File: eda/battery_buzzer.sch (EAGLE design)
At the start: 28 parts, among them Q2 IRFML8244, U1 ISL83491SOIC, U2 ATTINY1634

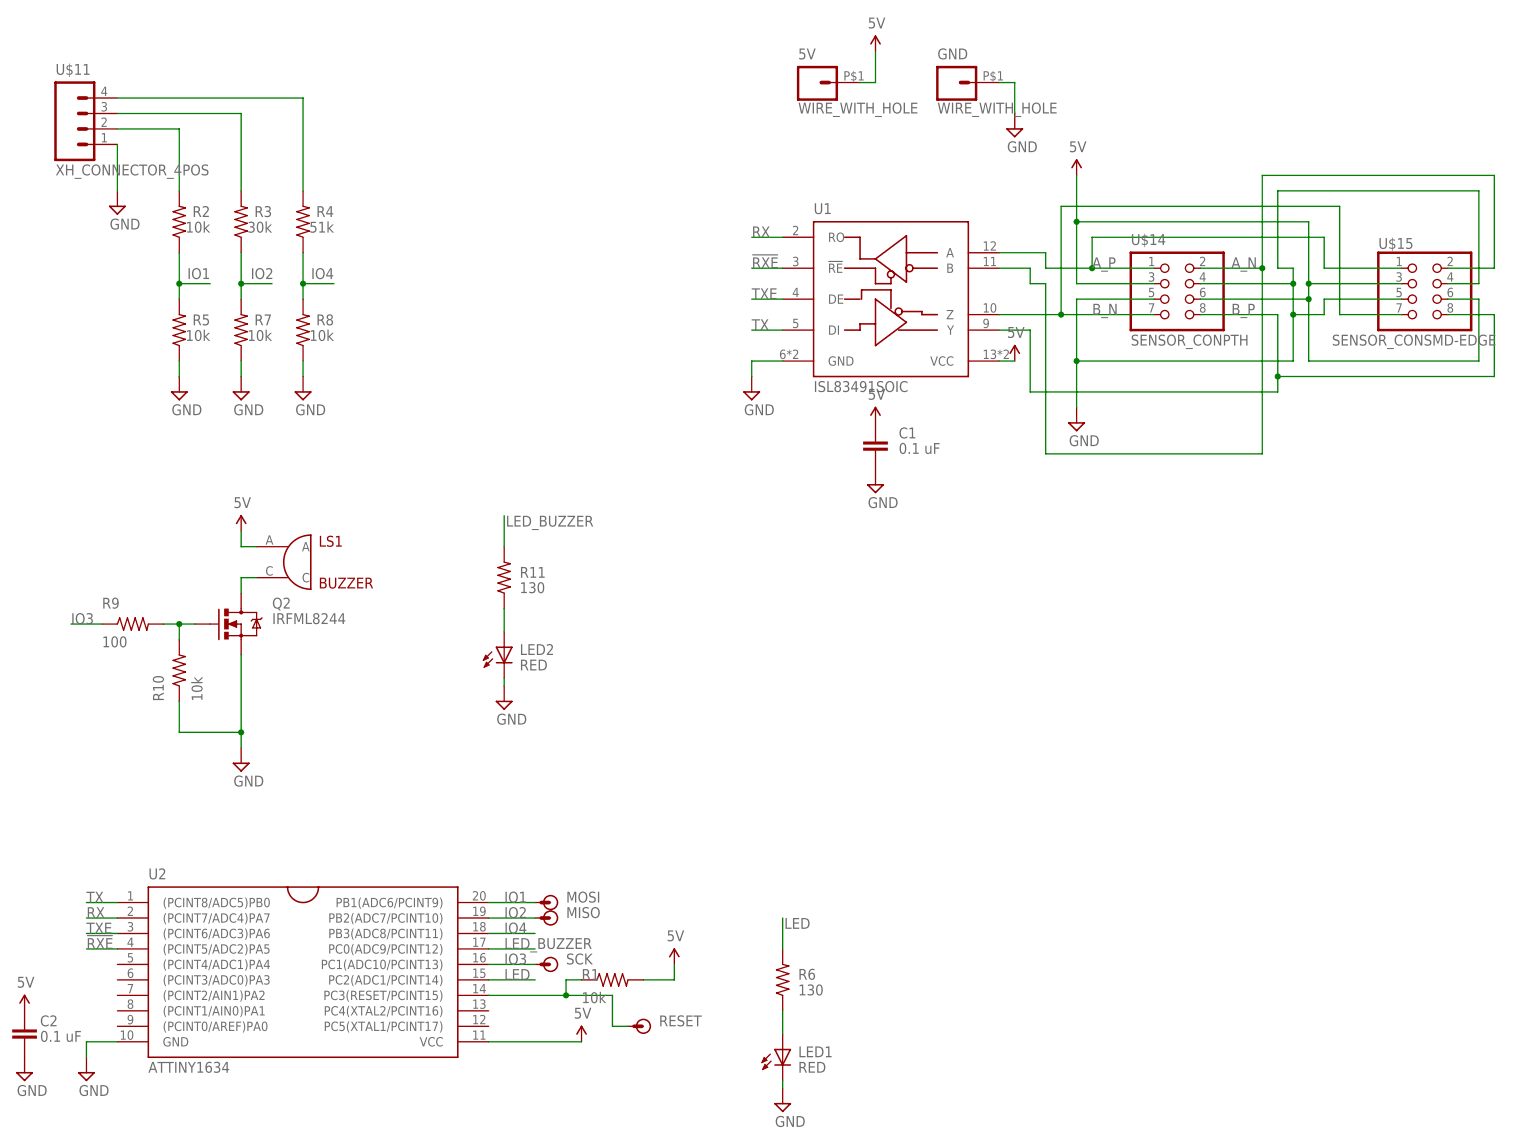
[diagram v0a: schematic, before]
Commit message: Change smartsensor connectors to 2x5
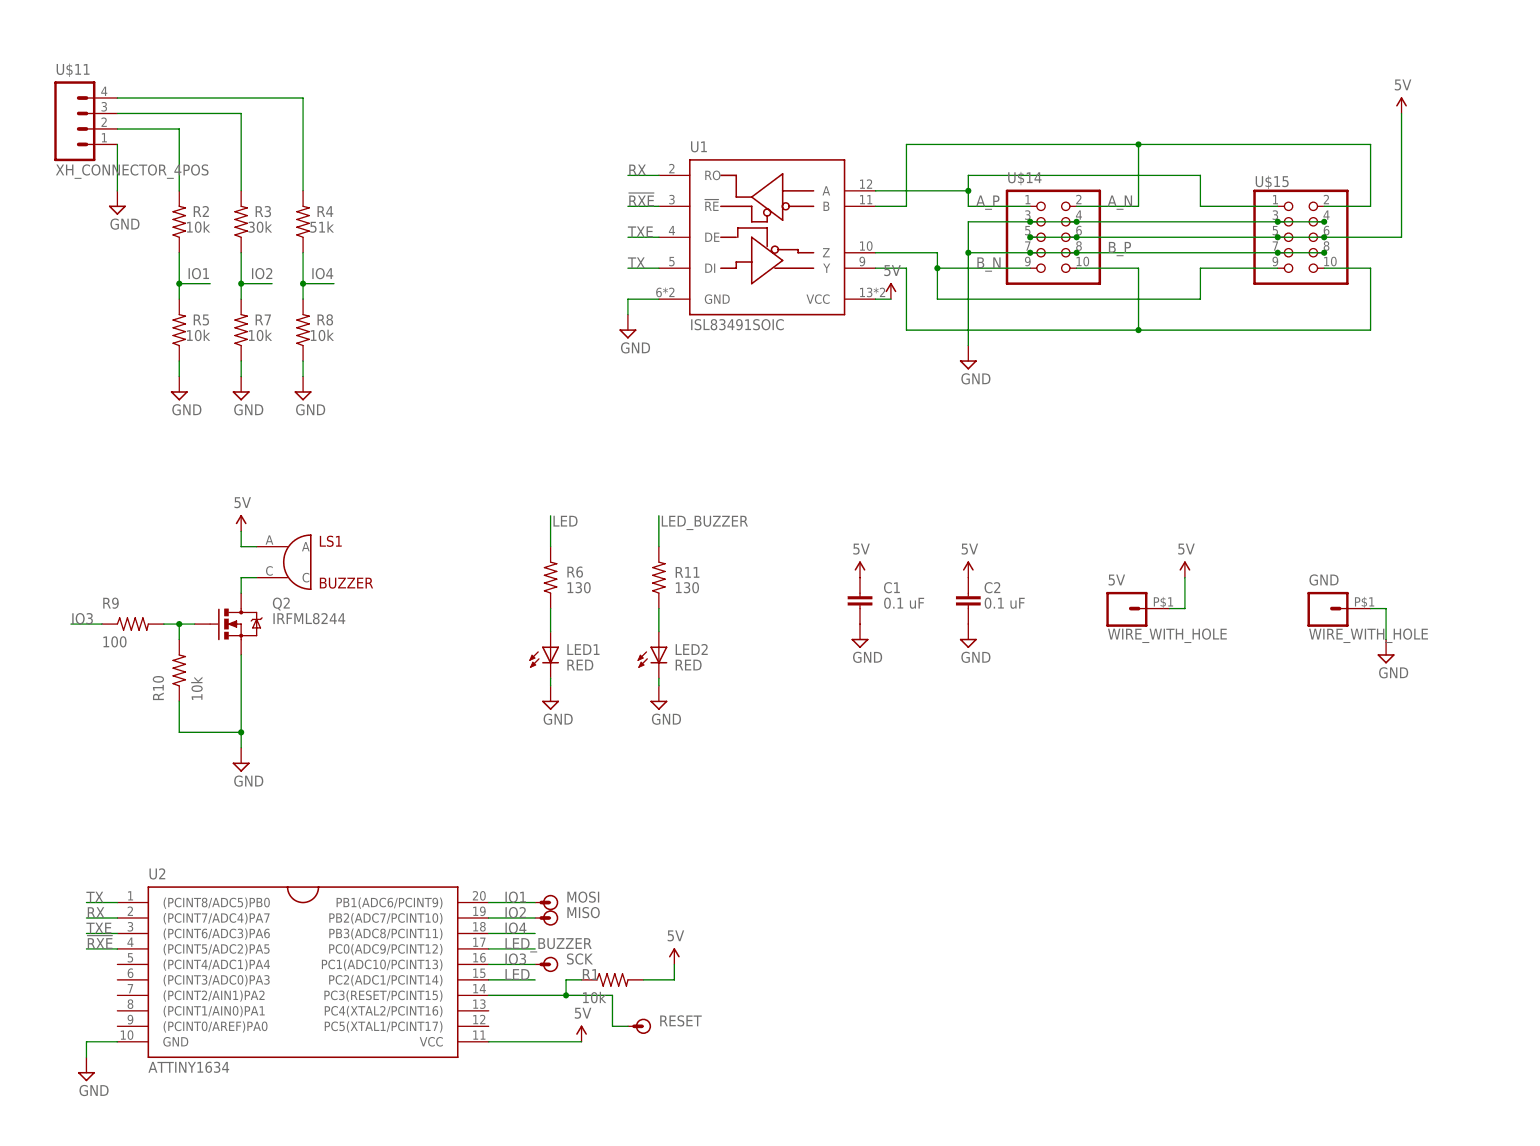
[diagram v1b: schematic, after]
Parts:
- U$14: value SENSOR_CONPTH -> (none); device pie:SENSOR_CONPTH -> pie:SENSOR_CON_5PINPTH
- U$15: value SENSOR_CONSMD-EDGE -> (none); device pie:SENSOR_CONSMD-EDGE -> pie:SENSOR_CON_5PINSMD-EDGE
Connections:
- net 5V: now also U$14.5, U$15.5; no longer U$14.3, U$15.3
- net B_N: now also U$14.9, U$15.9; no longer U$14.7, U$15.7
- net B_P: now also U$14.10, U$15.10; no longer U$14.8, U$15.8
- net GND: now also U$14.3, U$14.7, U$14.8, U$15.3, U$15.7, U$15.8; no longer U$14.5, U$15.5
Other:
- moved on the sheet: 5V, C1, C2, GND, LED1, LED2, R11, R6, U1
